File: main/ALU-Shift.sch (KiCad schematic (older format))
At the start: 6 parts, among them U43 74LS32, U44 74LS86, U45 74LS194, U46 74LS02, U47 74LS194, U48 74LS245

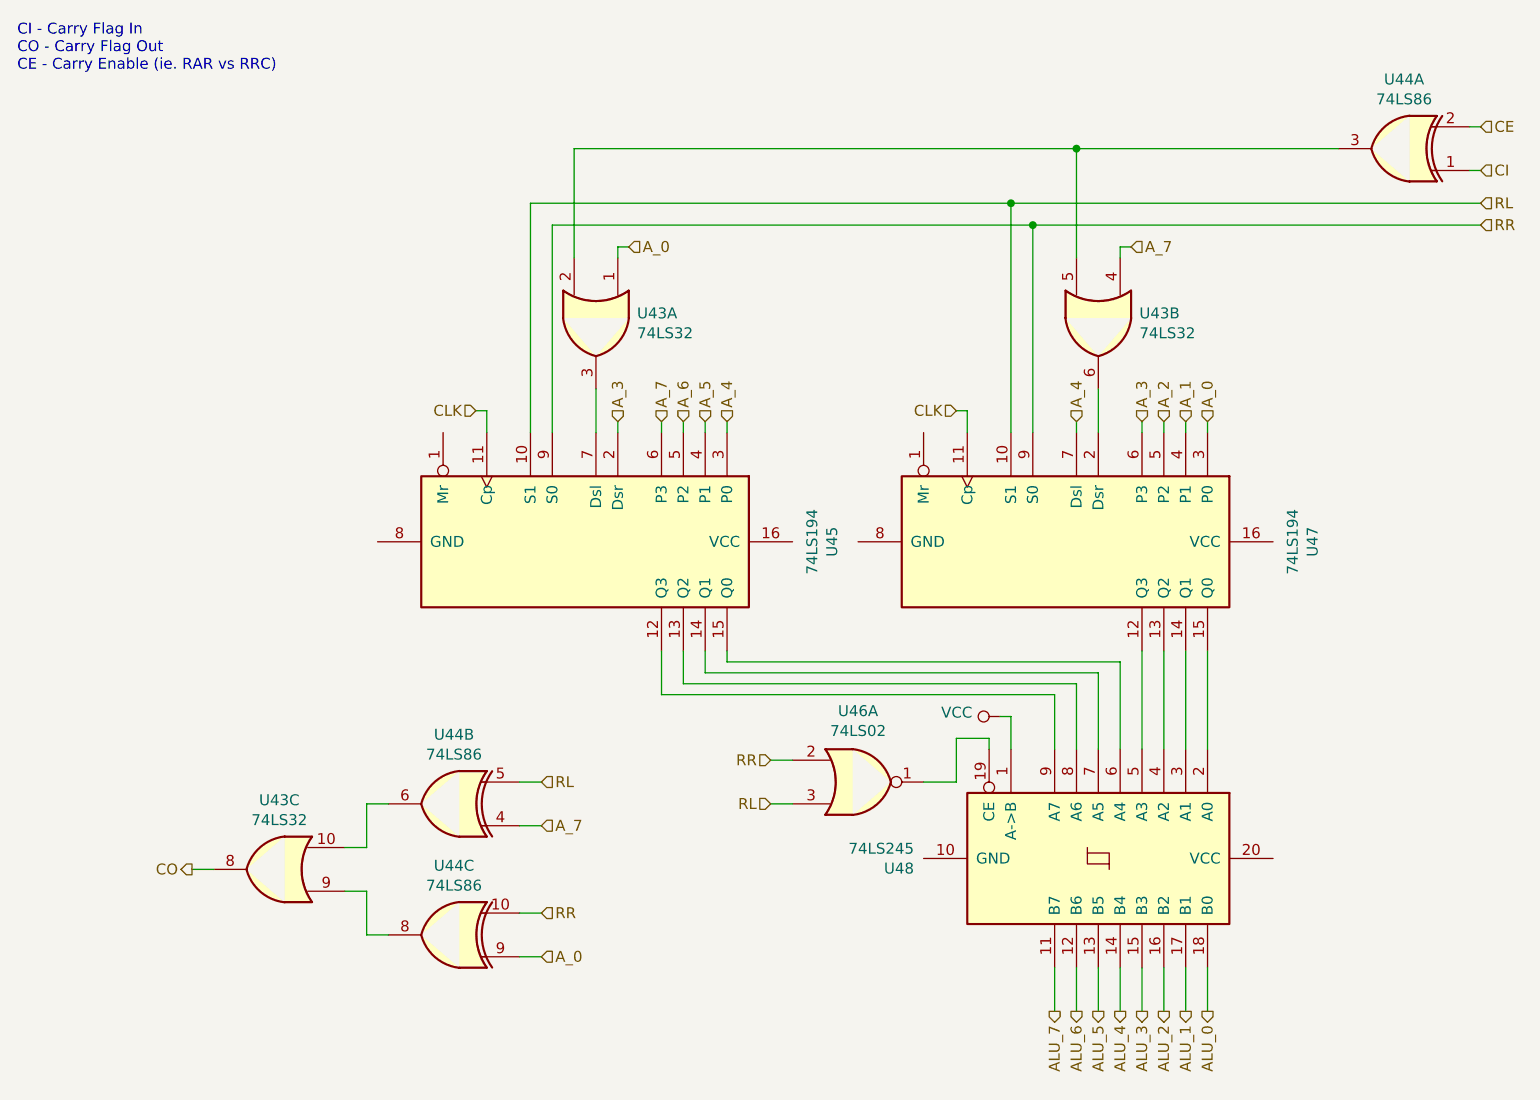
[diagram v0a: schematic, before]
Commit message: Replot main with symbols
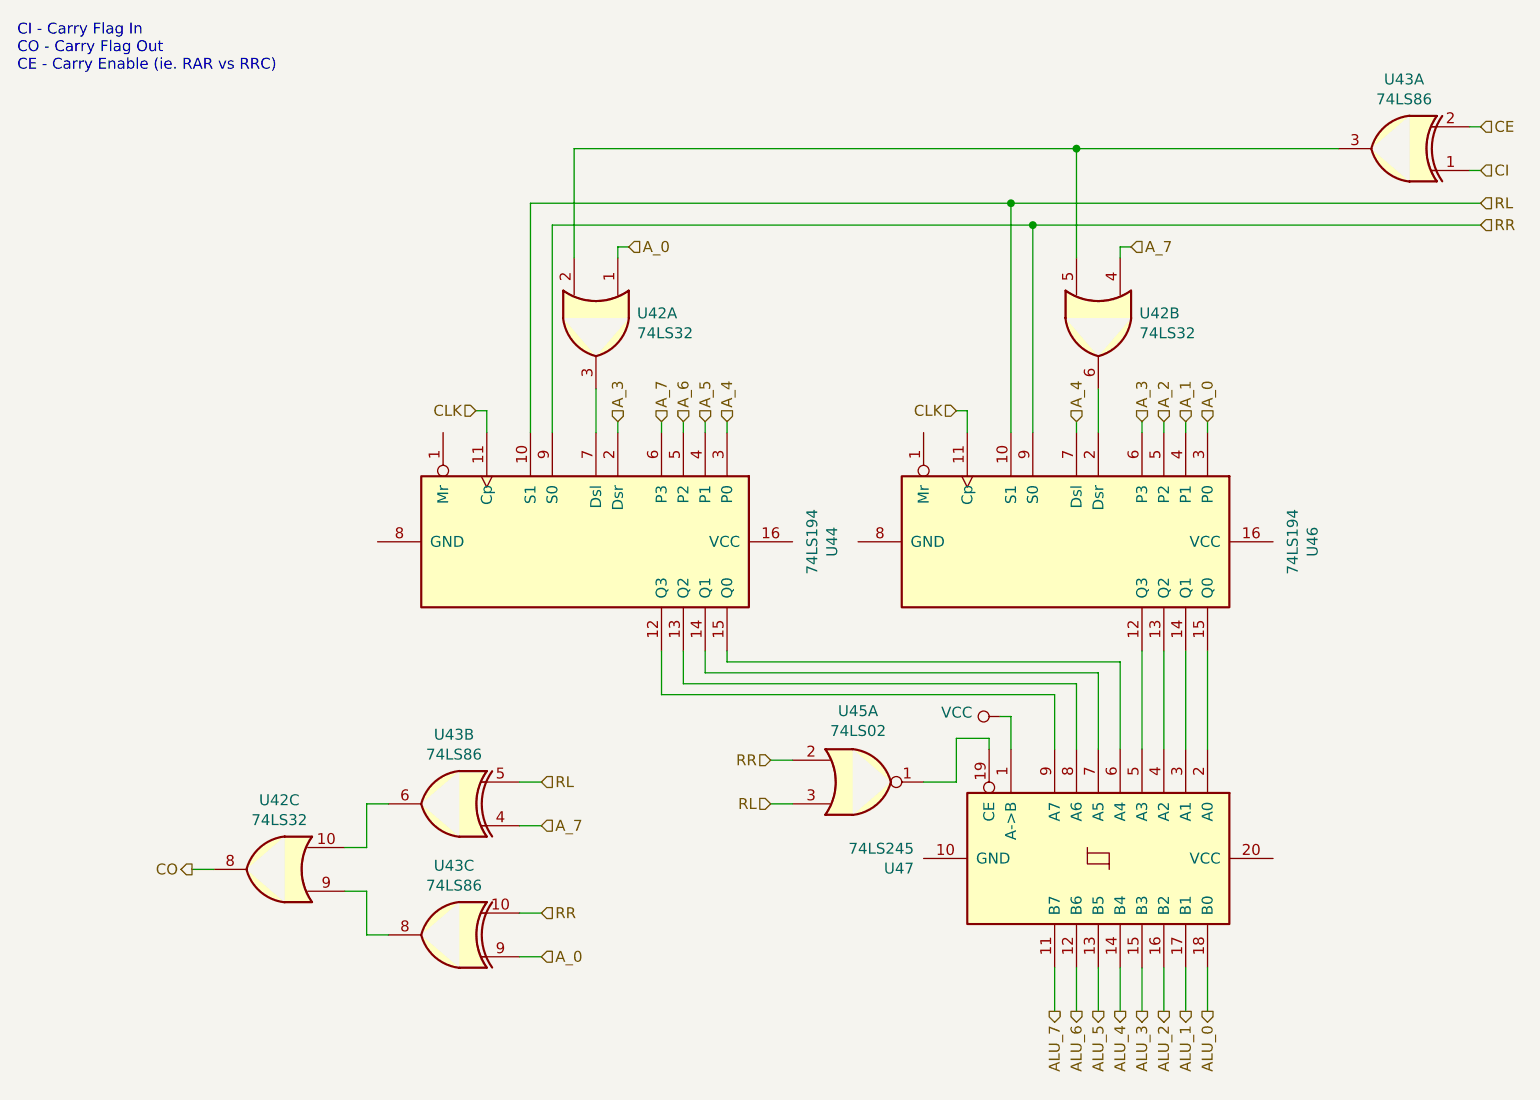
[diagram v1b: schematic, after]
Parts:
- renumbered U43 to U42, U44 to U43, U45 to U44, U46 to U45, U47 to U46, U48 to U47
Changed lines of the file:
@@
 Sheet 11 26
 Title "ALU Shifter"
-Date "2019-11-13"
+Date "2019-11-17"
 Rev "v1.0"
 Comp "Christopher Milan"
@@
 AR Path="/5E5B2E62/5DF0EA60" Ref="U?"  Part="1"
 AR Path="/5E5B2E62/5E0141CE/5DF0EA60" Ref="U?"  Part="1"
-AR Path="/5E5B2E62/5E0141CE/5DF0B9F6/5DF0EA60" Ref="U47"  Part="1"
-F 0 "U47" H 5950 4481 50  0000 C CNN
+AR Path="/5E5B2E62/5E0141CE/5DF0B9F6/5DF0EA60" Ref="U46"  Part="1"
+F 0 "U46" H 5950 4481 50  0000 C CNN
 F 1 "74LS194" H 5950 4390 50  0000 C CNN
 F 2 "" H 5950 3400 50  0001 C CNN
@@
 AR Path="/5E5B2E62/5DF0EA66" Ref="U?"  Part="1"
 AR Path="/5E5B2E62/5E0141CE/5DF0EA66" Ref="U?"  Part="1"
-AR Path="/5E5B2E62/5E0141CE/5DF0B9F6/5DF0EA66" Ref="U45"  Part="1"
-F 0 "U45" H 3750 4481 50  0000 C CNN
+AR Path="/5E5B2E62/5E0141CE/5DF0B9F6/5DF0EA66" Ref="U44"  Part="1"
+F 0 "U44" H 3750 4481 50  0000 C CNN
 F 1 "74LS194" H 3750 4390 50  0000 C CNN
 F 2 "" H 3750 3400 50  0001 C CNN
@@
 	3250 2800 3250 2900
 $Comp
-L 74xx:74LS86 U44
+L 74xx:74LS86 U43
 U 1 1 5DF678BA
 P 7450 1600
-F 0 "U44" H 7450 1283 50  0000 C CNN
+F 0 "U43" H 7450 1283 50  0000 C CNN
 F 1 "74LS86" H 7450 1374 50  0000 C CNN
 F 2 "" H 7450 1600 50  0001 C CNN
@@
 	3450 1850 3450 2900
 $Comp
-L 74xx:74LS32 U43
+L 74xx:74LS32 U42
 U 1 1 5E065035
 P 3750 2400
-F 0 "U43" V 3704 2588 50  0000 L CNN
+F 0 "U42" V 3704 2588 50  0000 L CNN
 F 1 "74LS32" V 3795 2588 50  0000 L CNN
 F 2 "" H 3750 2400 50  0001 C CNN
@@
 	3650 1600 3650 2100
 $Comp
-L 74xx:74LS32 U43
+L 74xx:74LS32 U42
 U 2 1 5E091AB1
 P 6050 2400
-F 0 "U43" V 6004 2588 50  0000 L CNN
+F 0 "U42" V 6004 2588 50  0000 L CNN
 F 1 "74LS32" V 6095 2588 50  0000 L CNN
 F 2 "" H 6050 2400 50  0001 C CNN
@@
 CO
 $Comp
-L 74xx:74LS32 U43
+L 74xx:74LS32 U42
 U 3 1 5E0B4DCA
 P 2300 4900
-F 0 "U43" H 2300 4583 50  0000 C CNN
+F 0 "U42" H 2300 4583 50  0000 C CNN
 F 1 "74LS32" H 2300 4674 50  0000 C CNN
 F 2 "" H 2300 4900 50  0001 C CNN
@@
 	2000 4900 1900 4900
 $Comp
-L 74xx:74LS86 U44
+L 74xx:74LS86 U43
 U 2 1 5E0BDF76
 P 3100 4600
-F 0 "U44" H 3100 4283 50  0000 C CNN
+F 0 "U43" H 3100 4283 50  0000 C CNN
 F 1 "74LS86" H 3100 4374 50  0000 C CNN
 F 2 "" H 3100 4600 50  0001 C CNN
@@
 	2700 4800 2600 4800
 $Comp
-L 74xx:74LS86 U44
+L 74xx:74LS86 U43
 U 3 1 5E0C532F
 P 3100 5200
-F 0 "U44" H 3100 4883 50  0000 C CNN
+F 0 "U43" H 3100 4883 50  0000 C CNN
 F 1 "74LS86" H 3100 4974 50  0000 C CNN
 F 2 "" H 3100 5200 50  0001 C CNN
@@
 AR Path="/5E5B2E62/5E164880" Ref="U?"  Part="1"
 AR Path="/5E5B2E62/5E0141CE/5D94D587/5E164880" Ref="U?"  Part="1"
-AR Path="/5E5B2E62/5E0141CE/5DF0B9F6/5E164880" Ref="U48"  Part="1"
-F 0 "U48" V 6096 4006 50  0000 R CNN
+AR Path="/5E5B2E62/5E0141CE/5DF0B9F6/5E164880" Ref="U47"  Part="1"
+F 0 "U47" V 6096 4006 50  0000 R CNN
 F 1 "74LS245" V 6005 4006 50  0000 R CNN
 F 2 "" H 6050 4850 50  0001 C CNN
@@
 	5550 4350 5550 4300
 $Comp
-L 74xx:74LS02 U46
+L 74xx:74LS02 U45
 U 1 1 5E1AFD0C
 P 4950 4500
-F 0 "U46" H 4950 4825 50  0000 C CNN
+F 0 "U45" H 4950 4825 50  0000 C CNN
 F 1 "74LS02" H 4950 4734 50  0000 C CNN
 F 2 "" H 4950 4500 50  0001 C CNN
